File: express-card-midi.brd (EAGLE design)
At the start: 18.9 x 65 mm, 1 part

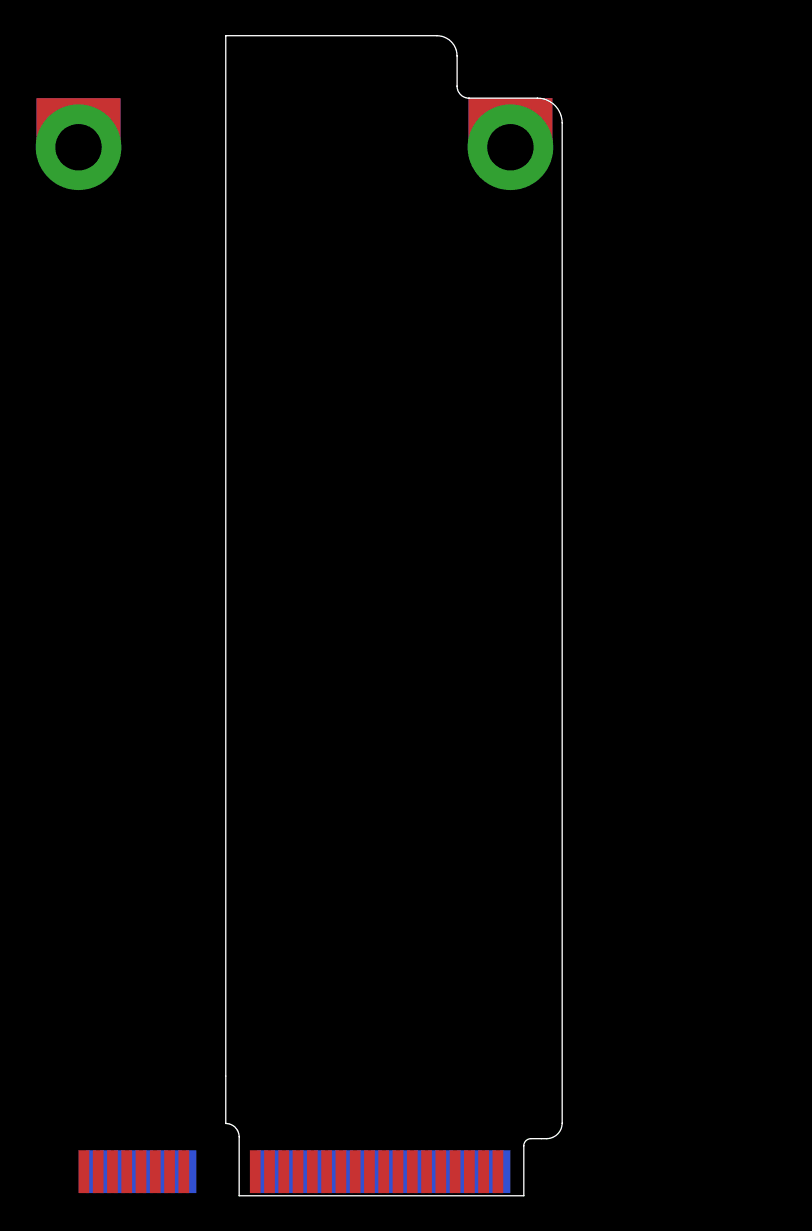
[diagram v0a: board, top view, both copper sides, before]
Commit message: board placement into positive values
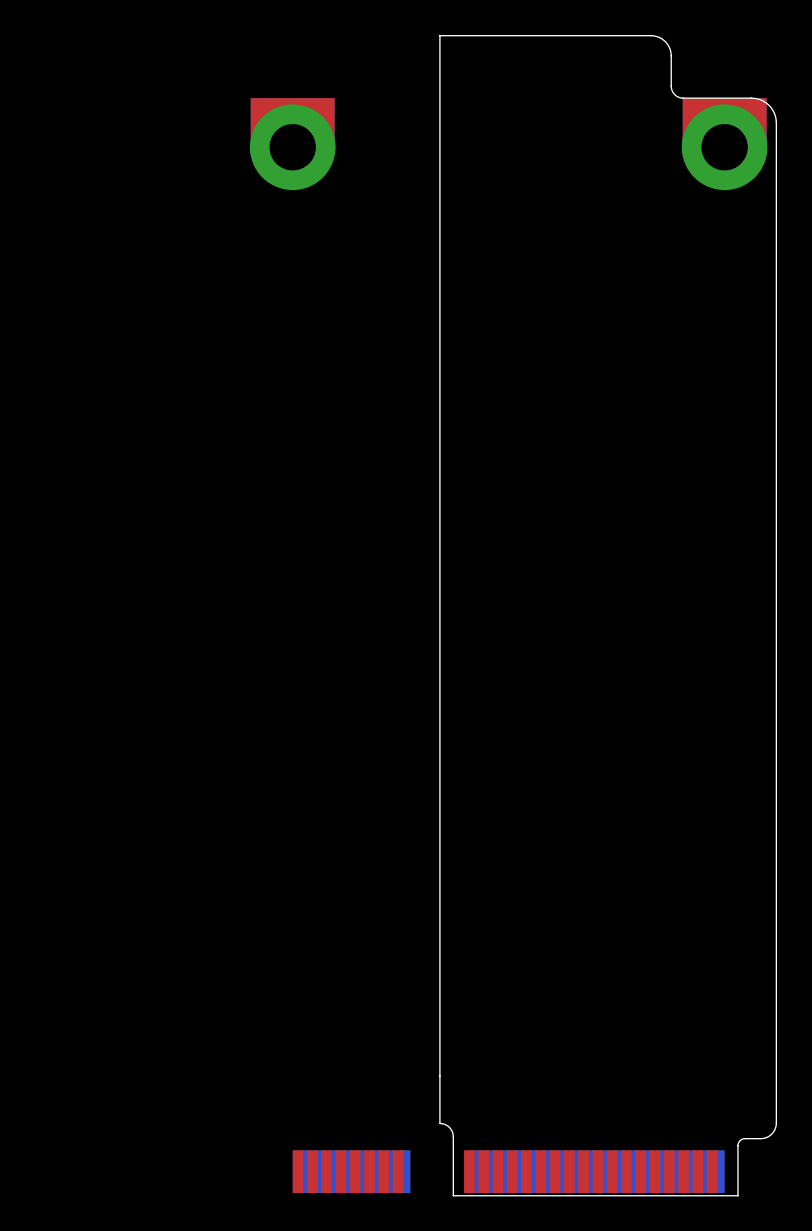
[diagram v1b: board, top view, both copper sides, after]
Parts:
- moved U$1 12.0 mm to (12.0, 0.00)
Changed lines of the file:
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@@
 <setting verticaltext="up"/>
 </settings>
-<grid distance="0.1" unitdist="mm" unit="mm" style="lines" multiple="1" display="yes" altdistance="0.025" altunitdist="inch" altunit="inch"/>
+<grid distance="1" unitdist="mm" unit="mm" style="lines" multiple="1" display="yes" altdistance="0.025" altunitdist="inch" altunit="inch"/>
 <layers>
 <layer number="1" name="Top" color="4" fill="1" visible="yes" active="yes"/>
@@
 <board>
 <plain>
-<wire x1="0.75" y1="0.1" x2="0.75" y2="3.4" width="0" layer="20"/>
-<wire x1="0" y1="4.15" x2="0.75" y2="3.4" width="0" layer="20" curve="-90"/>
-<wire x1="18.85" y1="60.20985625" x2="18.85" y2="4.173209375" width="0" layer="20"/>
-<wire x1="18.85" y1="4.173209375" x2="17.976790625" y2="3.3" width="0" layer="20" curve="-90"/>
-<wire x1="17.976790625" y1="3.3" x2="17.7" y2="3.3" width="0" layer="20"/>
-<wire x1="0.75" y1="0.1" x2="16.7" y2="0.1" width="0" layer="20"/>
-<wire x1="16.7" y1="0.1" x2="16.7" y2="2.9" width="0" layer="20"/>
-<wire x1="17.7" y1="3.3" x2="17.1" y2="3.3" width="0" layer="20"/>
-<wire x1="17.1" y1="3.3" x2="16.7" y2="2.9" width="0" layer="20" curve="90"/>
-<wire x1="18.85" y1="60.20985625" x2="17.45985625" y2="61.6" width="0" layer="20" curve="90"/>
-<wire x1="12.96" y1="63.967925" x2="12.96" y2="62.272009375" width="0" layer="20"/>
-<wire x1="12.96" y1="62.272009375" x2="13.632009375" y2="61.6" width="0" layer="20" curve="90"/>
-<wire x1="13.632009375" y1="61.6" x2="17.45985625" y2="61.6" width="0" layer="20"/>
-<wire x1="0" y1="65.1" x2="11.827925" y2="65.1" width="0" layer="20"/>
-<wire x1="11.827925" y1="65.1" x2="12.96" y2="63.967925" width="0" layer="20" curve="-90"/>
-<wire x1="0" y1="4.15" x2="0" y2="6.8" width="0" layer="20"/>
-<wire x1="0" y1="6.8" x2="0" y2="65.1" width="0" layer="20"/>
+<wire x1="12.75" y1="0.1" x2="12.75" y2="3.4" width="0" layer="20"/>
+<wire x1="12" y1="4.15" x2="12.75" y2="3.4" width="0" layer="20" curve="-90"/>
+<wire x1="30.85" y1="60.20985625" x2="30.85" y2="4.173209375" width="0" layer="20"/>
+<wire x1="30.85" y1="4.173209375" x2="29.976790625" y2="3.3" width="0" layer="20" curve="-90"/>
+<wire x1="29.976790625" y1="3.3" x2="29.7" y2="3.3" width="0" layer="20"/>
+<wire x1="12.75" y1="0.1" x2="28.7" y2="0.1" width="0" layer="20"/>
+<wire x1="28.7" y1="0.1" x2="28.7" y2="2.9" width="0" layer="20"/>
+<wire x1="29.7" y1="3.3" x2="29.1" y2="3.3" width="0" layer="20"/>
+<wire x1="29.1" y1="3.3" x2="28.7" y2="2.9" width="0" layer="20" curve="90"/>
+<wire x1="30.85" y1="60.20985625" x2="29.45985625" y2="61.6" width="0" layer="20" curve="90"/>
+<wire x1="24.96" y1="63.967925" x2="24.96" y2="62.272009375" width="0" layer="20"/>
+<wire x1="24.96" y1="62.272009375" x2="25.632009375" y2="61.6" width="0" layer="20" curve="90"/>
+<wire x1="25.632009375" y1="61.6" x2="29.45985625" y2="61.6" width="0" layer="20"/>
+<wire x1="12" y1="65.1" x2="23.827925" y2="65.1" width="0" layer="20"/>
+<wire x1="23.827925" y1="65.1" x2="24.96" y2="63.967925" width="0" layer="20" curve="-90"/>
+<wire x1="12" y1="4.15" x2="12" y2="6.8" width="0" layer="20"/>
+<wire x1="12" y1="6.8" x2="12" y2="65.1" width="0" layer="20"/>
 </plain>
 <attributes>
@@
 </autorouter>
 <elements>
-<element name="U$1" library="teensy-express" package="FULL-MINI-PCI-E" value="FULL-MINI-PCI-E" x="0" y="0"/>
+<element name="U$1" library="teensy-express" package="FULL-MINI-PCI-E" value="FULL-MINI-PCI-E" x="12" y="0"/>
 </elements>
 <signals>
@@
 <contactref element="U$1" pad="LATCH@1"/>
 <contactref element="U$1" pad="LATCH@2"/>
-<wire x1="-8.25" y1="58.85" x2="15.95" y2="58.85" width="0" layer="19" extent="1-1"/>
+<wire x1="3.75" y1="58.85" x2="27.95" y2="58.85" width="0" layer="19" extent="1-1"/>
 </signal>
 </signals>
